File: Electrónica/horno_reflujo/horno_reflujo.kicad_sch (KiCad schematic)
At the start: 51 parts, among them J1 Jack-DC, J2 5V USB cargador, J3 Nextion_touch_screen, J4 Max6675_modulo, J5 ESP01, J6 Alimentación y zc, J7 Relevador a ventilador, J8 Tarjeta a SSR, J9 SSR a resistencias, K1 SANYOU_SRD_Form_C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

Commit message: stm32 reflow_oven proyecto
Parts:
- R5, R6: value 5k 1W -> 5k 2W
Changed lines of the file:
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@@
 			)
 		)
-		(property "Value" "5k  1W"
+		(property "Value" "5k  2W"
 			(at 185.42 78.74 90)
 			(effects
@@
 			)
 		)
-		(property "Value" "5k  1W"
+		(property "Value" "5k  2W"
 			(at 186.69 53.34 90)
 			(effects

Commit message: pcb updated :)
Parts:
- removed C3, C7: 1uf, Capacitor_THT:CP_Radial_D5.0mm_P2.50mm, symbol Device:C_Polarized_US
- removed C4, C6: 10uf, Capacitor_THT:CP_Radial_D5.0mm_P2.50mm, symbol Device:C_Polarized_US
- removed J1: Jack-DC, symbol Connector:Jack-DC
- removed J2: 5V USB cargador, Connector_PinHeader_2.54mm:PinHeader_1x02_P2.54mm_Vertical, symbol Connector:Conn_01x02_Socket
- removed J8: Tarjeta a SSR, TerminalBlock:TerminalBlock_Xinya_XY308-2.54-2P_1x02_P2.54mm_Horizontal, symbol Connector:Screw_Terminal_01x02
- removed J9: SSR a resistencias, TerminalBlock:TerminalBlock_Xinya_XY308-2.54-2P_1x02_P2.54mm_Horizontal, symbol Connector:Screw_Terminal_01x02
- removed R1, R2, R3, R4: 10, symbol Device:Heater
- removed R11, R8: 1K, symbol Device:R_US
- removed R12, R9: 2K, symbol Device:R_US
- removed U1: SSR-40 DA, Relay_THT:Relay_NCR_HHG1D-1, symbol Relay_SolidState:HHG1D-1
- removed U2: LM7805CT, PCM_Package_TO_SOT_THT_AKL:TO-220-3_Vertical, symbol PCM_Voltage_Regulator_AKL:LM7805CT
- removed unit 4 of U3
- removed unit 5 of U3
- removed unit 3 of U3
- removed U5: ESP-01S, RF_Module:ESP-01, symbol speedy_hardware_items:ESP-01s
- added J1, J2: LevelShifter, Connector_PinHeader_2.54mm:PinHeader_1x06_P2.54mm_Vertical, symbol Connector:Conn_01x06_Pin
- added J10: ssr1, TerminalBlock:TerminalBlock_Xinya_XY308-2.54-2P_1x02_P2.54mm_Horizontal, symbol Connector:Screw_Terminal_01x02
- added J11: ssr2, TerminalBlock:TerminalBlock_Xinya_XY308-2.54-2P_1x02_P2.54mm_Horizontal, symbol Connector:Screw_Terminal_01x02
- added J12: encoder, Connector_PinHeader_2.54mm:PinHeader_1x05_P2.54mm_Vertical, symbol Connector:Conn_01x05_Pin
- added J13: Max6675_modulo2, Connector_PinHeader_2.54mm:PinHeader_1x05_P2.54mm_Vertical, symbol Connector:Conn_01x05_Pin
- added J14: Max6675_modulo3, Connector_PinHeader_2.54mm:PinHeader_1x05_P2.54mm_Vertical, symbol Connector:Conn_01x05_Pin
- added J15: Max6675_modulo4, Connector_PinHeader_2.54mm:PinHeader_1x05_P2.54mm_Vertical, symbol Connector:Conn_01x05_Pin
- added J8: resistencia, Connector_PinHeader_2.54mm:PinHeader_1x01_P2.54mm_Vertical, symbol Connector:Conn_01x01_Pin
- added J9: resistencia1, Connector_PinHeader_2.54mm:PinHeader_1x01_P2.54mm_Vertical, symbol Connector:Conn_01x01_Pin
- C2, C5: footprint (none) -> Capacitor_THT:C_Disc_D5.1mm_W3.2mm_P5.00mm
- D1: footprint PCM_Diode_THT_AKL:Diode_Bridge_Round_D9.8mm -> Diode_THT:Diode_Bridge_Round_D9.0mm
- D3: footprint PCM_Diode_THT_AKL:D_DO-41_SOD81_P7.62mm_Horizontal -> Diode_THT:D_A-405_P10.16mm_Horizontal
- F1, F2, F3: footprint Fuse:Fuseholder_Clip-5x20mm_Schurter_OG_Lateral_P15.00x5.00mm_D1.3mm_Horizontal -> Fuse:Fuseholder_Cylinder-5x20mm_Schurter_0031_8201_Horizontal_Open
- J3: value Nextion_touch_screen -> Display Oled I2C; footprint Connector_PinHeader_2.54mm:PinHeader_1x04_P2.54mm_Horizontal -> Connector_PinHeader_2.54mm:PinHeader_1x04_P2.54mm_Vertical
- J4: footprint Connector_PinHeader_2.54mm:PinHeader_1x05_P2.54mm_Horizontal -> Connector_PinHeader_2.54mm:PinHeader_1x05_P2.54mm_Vertical
- J5: footprint Connector_PinHeader_2.54mm:PinHeader_1x04_P2.54mm_Horizontal -> Connector_PinHeader_2.54mm:PinHeader_1x04_P2.54mm_Vertical
- OC1: footprint PCM_Package_DIP_AKL:DIP-4_W7.62mm_LongPads -> Package_DIP:DIP-4_W10.16mm
- Q1: footprint PCM_Package_TO_SOT_THT_AKL:TO-92_Inline_Wide -> Package_TO_SOT_THT:TO-92
- R10, R7: footprint (none) -> Resistor_THT:R_Axial_DIN0204_L3.6mm_D1.6mm_P7.62mm_Horizontal
- R5, R6: value 5k 2W -> 5k 1W
- RV1: footprint (none) -> Varistor:RV_Disc_D7mm_W4.2mm_P5mm
- U3: footprint Package_DIP:DIP-14_W7.62mm_Socket_LongPads -> (none)
- U4: footprint PCM_Package_TO_SOT_THT_AKL:TO-220-3_Vertical -> Package_TO_SOT_THT:TO-220-3_Vertical
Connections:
- net cs is gone; now on net CS_0: J4.4 (Pin_4)
- net sck is gone; now on net SPI1_SCK: J4.3 (Pin_3)
- net so is gone; now on net SPI1_MISO: J4.5 (Pin_5)
- net +3.3V: now also J4.2 (Pin_2), J1.4 (Pin_4), J13.2 (Pin_2), J14.2 (Pin_2), J15.2 (Pin_2)
- net +5V: now also J2.3 (Pin_3); no longer J4.2 (Pin_2)
- net GND: now also J1.3 (Pin_3), J10.2 (Pin_2), J12.4 (Pin_4), J12.5 (Pin_5), J13.1 (Pin_1), J14.1 (Pin_1), J15.1 (Pin_1), J2.4 (Pin_4)
- net NEUT: now also J11.1 (Pin_1)
- net Rx_mcu_esp01: now also dev_board1.10 (A15)
- net Tx_mcu_esp01: now also dev_board1.7 (A10)
- net fan: now also dev_board1.8 (A11)
- net fire: now also dev_board1.6 (A9)
- net zc: now also dev_board1.5 (A8), J1.2 (Pin_2)
- net I2C1_SCL: now reaches dev_board1.14 (B6)
- net I2C1_SCL: now also J1.6 (Pin_6)
- net I2C1_SDA: now reaches dev_board1.15 (B7)
- net I2C1_SDA: now also J1.5 (Pin_5)
- net built_in_led: now reaches dev_board1.22 (C13)
- net ENCODER_A: now reaches dev_board1.26 (A0)
- net ENCODER_A: now also J12.3 (Pin_3)
- net ENCODER_B: now reaches dev_board1.27 (A1)
- net ENCODER_B: now also J12.2 (Pin_2)
- net ENCODER_BTN: now reaches dev_board1.28 (A2)
- net ENCODER_BTN: now also J12.1 (Pin_1)
- net SPI1_SCK: now reaches dev_board1.31 (A5)
- net SPI1_SCK: now also J13.3 (Pin_3), J14.3 (Pin_3), J15.3 (Pin_3)
- net SPI1_MISO: now reaches dev_board1.32 (A6)
- net SPI1_MISO: now also J13.5 (Pin_5), J14.5 (Pin_5), J15.5 (Pin_5)
- net CS_0: now reaches dev_board1.33 (A7)
- net CS_1: now reaches dev_board1.34 (B0)
- net CS_1: now also J13.4 (Pin_4)
- net CS_2: now reaches dev_board1.35 (B1)
- net CS_2: now also J14.4 (Pin_4)
- net CS_3: now reaches dev_board1.36 (B2)
- net CS_3: now also J15.4 (Pin_4)
- net at F3.2: now also J9.1 (Pin_1)
- net at J3.3 (Pin_3): now also J2.2 (Pin_2)
- net at J3.2 (Pin_2): now also J2.1 (Pin_1)
- net at F2.2: now also J8.1 (Pin_1)
- net zero: now reaches U3.2
- net zero: now also J2.5 (Pin_5)
- net SSR_led: no longer names the net of U3.4
- net SSR_led: now also J10.1 (Pin_1)
- no-connect marks 8 -> 6
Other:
- moved on the sheet: J3, J4, J5

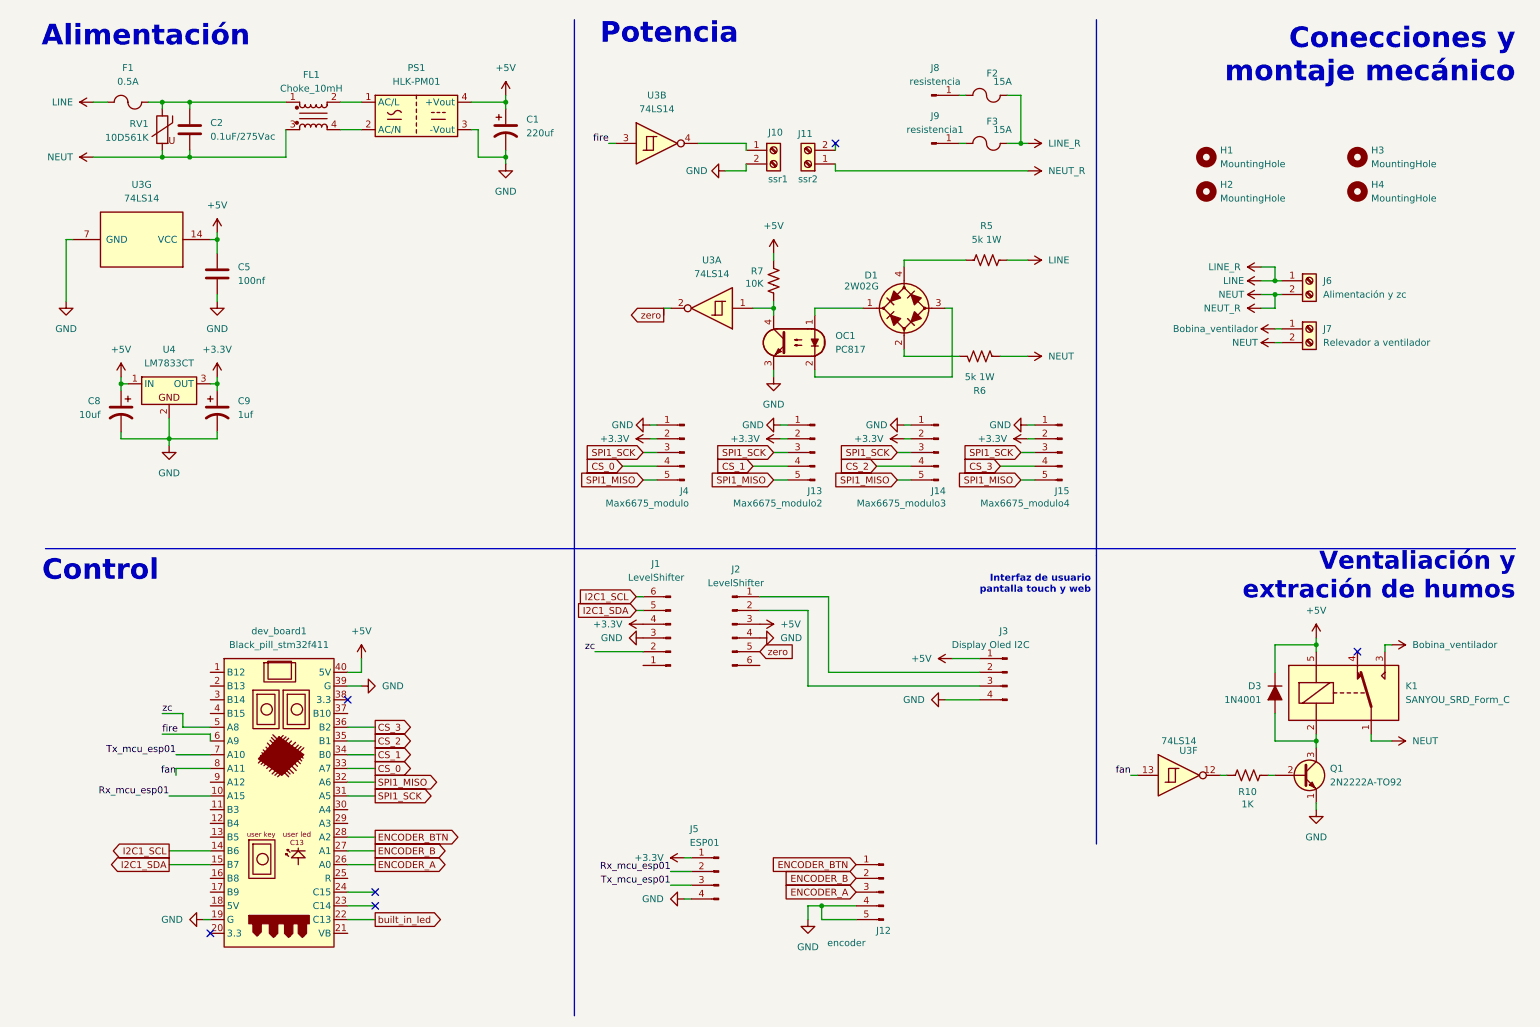
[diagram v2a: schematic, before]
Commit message: redesigned pcb
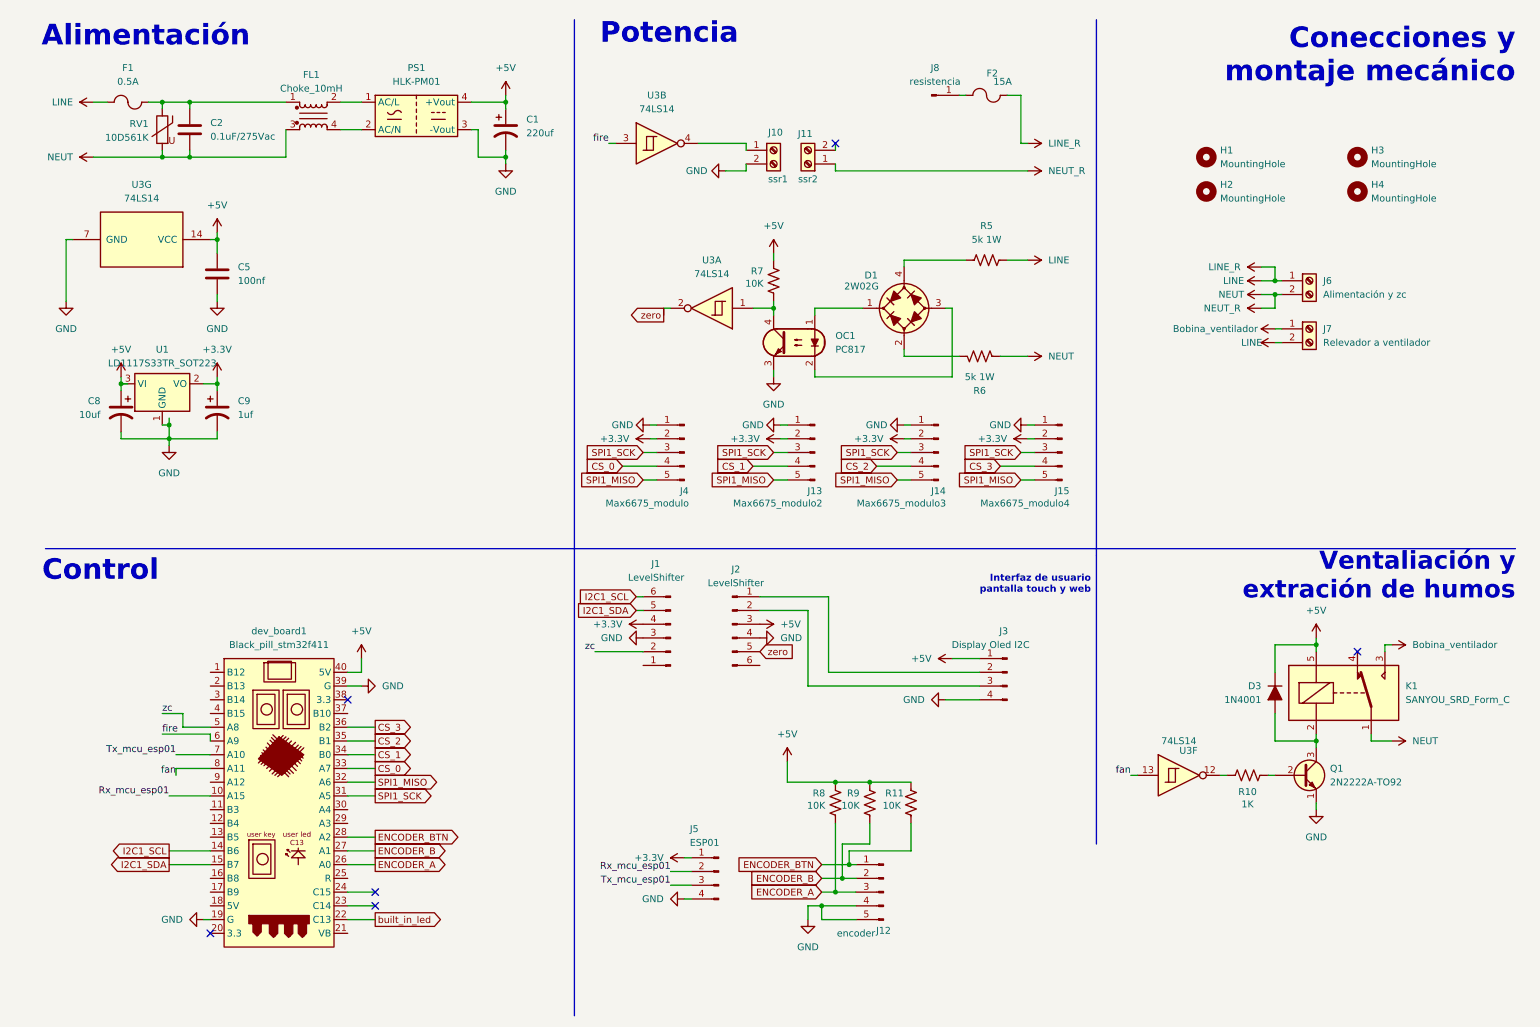
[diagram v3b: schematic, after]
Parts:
- removed F3: 15A, Fuse:Fuseholder_Cylinder-5x20mm_Schurter_0031_8201_Horizontal_Open, symbol PCM_Device_AKL:Fuse
- removed J9: resistencia1, Connector_PinHeader_2.54mm:PinHeader_1x01_P2.54mm_Vertical, symbol Connector:Conn_01x01_Pin
- removed U4: LM7833CT, Package_TO_SOT_THT:TO-220-3_Vertical, symbol PCM_Voltage_Regulator_AKL:LM7805CT
- added R11, R8, R9: 10K, Resistor_THT:R_Axial_DIN0204_L3.6mm_D1.6mm_P7.62mm_Horizontal, symbol Device:R_US
- added U1: LD1117S33TR_SOT223, Package_TO_SOT_SMD:SOT-223-3_TabPin2, symbol Regulator_Linear:LD1117S33TR_SOT223
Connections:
- net +3.3V: now also U1.2 (VO)
- net +5V: now also R11.2, R8.2, R9.2, U1.3 (VI)
- net ENCODER_A: now also R8.1
- net ENCODER_B: now also R9.1
- net ENCODER_BTN: now also R11.1
- net GND: now also U1.1 (GND)
- net LINE: now also J7.2 (Pin_2)
- net NEUT: no longer J7.2 (Pin_2)

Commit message: reorganizacion de folders
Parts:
- removed U3: 74LS14, symbol 74xx:74LS14
- added U2: 74LS14, Package_DIP:DIP-14_W7.62mm_Socket_LongPads, symbol 74xx:74LS14
- H1, H2, H3, H4: footprint MountingHole:MountingHole_2.2mm_M2_DIN965 -> MountingHole:MountingHole_3.2mm_M3_DIN965
- J10, J11, J6, J7: footprint TerminalBlock:TerminalBlock_Xinya_XY308-2.54-2P_1x02_P2.54mm_Horizontal -> TerminalBlock:TerminalBlock_bornier-2_P5.08mm
- R10, R11, R7, R8, R9: footprint Resistor_THT:R_Axial_DIN0204_L3.6mm_D1.6mm_P7.62mm_Horizontal -> Resistor_THT:R_Axial_DIN0207_L6.3mm_D2.5mm_P2.54mm_Vertical
- R5, R6: footprint Resistor_THT:R_Axial_DIN0411_L9.9mm_D3.6mm_P15.24mm_Horizontal -> Resistor_THT:R_Axial_DIN0411_L9.9mm_D3.6mm_P5.08mm_Vertical
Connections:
- net +3.3V: no longer J13.2 (Pin_2), J14.2 (Pin_2), J15.2 (Pin_2), J4.2 (Pin_2)
- net +5V: now also U2.14 (VCC)
- net GND: now also U2.7 (GND)
- net LINE: now also J6.2 (Pin_2); no longer J6.1 (Pin_1), R5.2
- net NEUT: now also J6.1 (Pin_1); no longer J6.2 (Pin_2)
- net fan: now also U2.3
- net fire: now also U2.5
- net zero: now also U2.2
- net +3.3Vmc: now reaches dev_board1.38 (3.3)
- net +3.3Vmc: now also J13.2 (Pin_2), J14.2 (Pin_2), J15.2 (Pin_2), J4.2 (Pin_2)
- net at J10.1 (Pin_1): now also U2.6
- net at F2.2, J8.1 (Pin_1): now also R5.2
- net at OC1.4, R7.1: now also U2.1
- net at R10.2: now also U2.4
- no-connect marks 6 -> 11
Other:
- moved on the sheet: C5

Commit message: mounting holes update
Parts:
- removed J8: resistencia, Connector_PinHeader_2.54mm:PinHeader_1x01_P2.54mm_Vertical, symbol Connector:Conn_01x01_Pin
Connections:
- net at F2.2, R5.2: now also J11.2 (Pin_2)
- no-connect marks 11 -> 10
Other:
- note added: "resistence"
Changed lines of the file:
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@@
 		)
 	)
+	(text "resistence "
+		(exclude_from_sim no)
+		(at 164.592 36.576 0)
+		(effects
+			(font
+				(size 1.27 1.27)
+			)
+		)
+	)
 	(text "Conecciones y\nmontaje mecánico\n"
 		(exclude_from_sim no)
@@
 	)
 	(no_connect
-		(at 158.75 35.56)
-	)
-	(no_connect
 		(at 234.95 97.79)
 	)
@@
 	(wire
 		(pts
-			(xy 200.66 49.53) (xy 200.66 36.83)
+			(xy 200.66 49.53) (xy 200.66 38.1)
 		)
 		(stroke
@@
 	(wire
 		(pts
+			(xy 158.75 26.67) (xy 182.88 26.67)
+		)
+		(stroke
+			(width 0)
+			(type default)
+		)
+	)
+	(wire
+		(pts
 			(xy 147.32 92.71) (xy 149.86 92.71)
 		)
@@
 	(wire
 		(pts
-			(xy 181.61 26.67) (xy 182.88 26.67)
-		)
-		(stroke
-			(width 0)
-			(type default)
-		)
-	)
-	(wire
-		(pts
 			(xy 68.58 151.13) (xy 73.66 151.13)
 		)
@@
 	(wire
 		(pts
-			(xy 158.75 35.56) (xy 158.75 36.83)
+			(xy 158.75 26.67) (xy 158.75 36.83)
 		)
 		(stroke
@@
 	(wire
 		(pts
-			(xy 182.88 36.83) (xy 182.88 26.67)
+			(xy 182.88 38.1) (xy 182.88 26.67)
 		)
 		(stroke
@@
 	(wire
 		(pts
-			(xy 200.66 36.83) (xy 182.88 36.83)
+			(xy 200.66 38.1) (xy 182.88 38.1)
 		)
 		(stroke
@@
 					(unit 1)
 				)
-			)
-		)
-	)
-	(symbol
-		(lib_id "Connector:Conn_01x01_Pin")
-		(at 176.53 26.67 0)
-		(unit 1)
-		(exclude_from_sim no)
-		(in_bom yes)
-		(on_board yes)
-		(dnp no)
-		(fields_autoplaced yes)
-		(property "Reference" "J8"
-			(at 177.165 21.59 0)
-			(effects
-				(font
-					(size 1.27 1.27)
-				)
-			)
-		)
-		(property "Value" "resistencia"
-			(at 177.165 24.13 0)
-			(effects
-				(font
-					(size 1.27 1.27)
-				)
-			)
-		)
-		(property "Footprint" "Connector_PinHeader_2.54mm:PinHeader_1x01_P2.54mm_Vertical"
-			(at 176.53 26.67 0)
-			(effects
-				(font
-					(size 1.27 1.27)
-				)
-				(hide yes)
-			)
-		)
-		(property "Datasheet" "~"
-			(at 176.53 26.67 0)
-			(effects
-				(font
-					(size 1.27 1.27)
-				)
-				(hide yes)
-			)
-		)
-		(property "Description" "Generic connector, single row, 01x01, script generated"
-			(at 176.53 26.67 0)
-			(effects
-				(font
-					(size 1.27 1.27)
-				)
-				(hide yes)
-			)
-		)
-		(pin "1"
-		)
-		(instances
-			(project ""
-				(path "/1b1a784e-59ad-41a0-994e-bee51370b96a"
-					(reference "J8")
-					(unit 1)
-				)

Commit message: actualizacion de placa
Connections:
- net +3.3V: now also J1.3 (Pin_3); no longer J1.4 (Pin_4)
- net +5V: now also J2.4 (Pin_4), J3.2 (Pin_2); no longer J2.3 (Pin_3), J3.1 (Pin_1)
- net GND: now also J1.4 (Pin_4), J2.3 (Pin_3), J3.1 (Pin_1); no longer J1.3 (Pin_3), J2.4 (Pin_4), J3.4 (Pin_4)
- net Rx_mcu_esp01: now also dev_board1.7 (A10); no longer dev_board1.10 (A15)
- net Tx_mcu_esp01: now also dev_board1.6 (A9); no longer dev_board1.7 (A10)
- net fire: now also dev_board1.5 (A8); no longer dev_board1.6 (A9)
- net zc: now also dev_board1.9 (A12); no longer dev_board1.5 (A8)
- net at J2.1 (Pin_1): now also J3.3 (Pin_3); no longer J3.2 (Pin_2)
- net at J2.2 (Pin_2): now also J3.4 (Pin_4); no longer J3.3 (Pin_3)
